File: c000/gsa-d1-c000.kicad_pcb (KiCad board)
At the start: 2 copper layers, 99.7 x 33 mm, 29 parts, among them J301 CONN-4, J302 CONN-3, J303 CONN-3, J304 CONN-3, J305 CONN-3, J306 CONN-3, J307 CONN-2, J308 CONN-3, U301 4066, U302 4066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

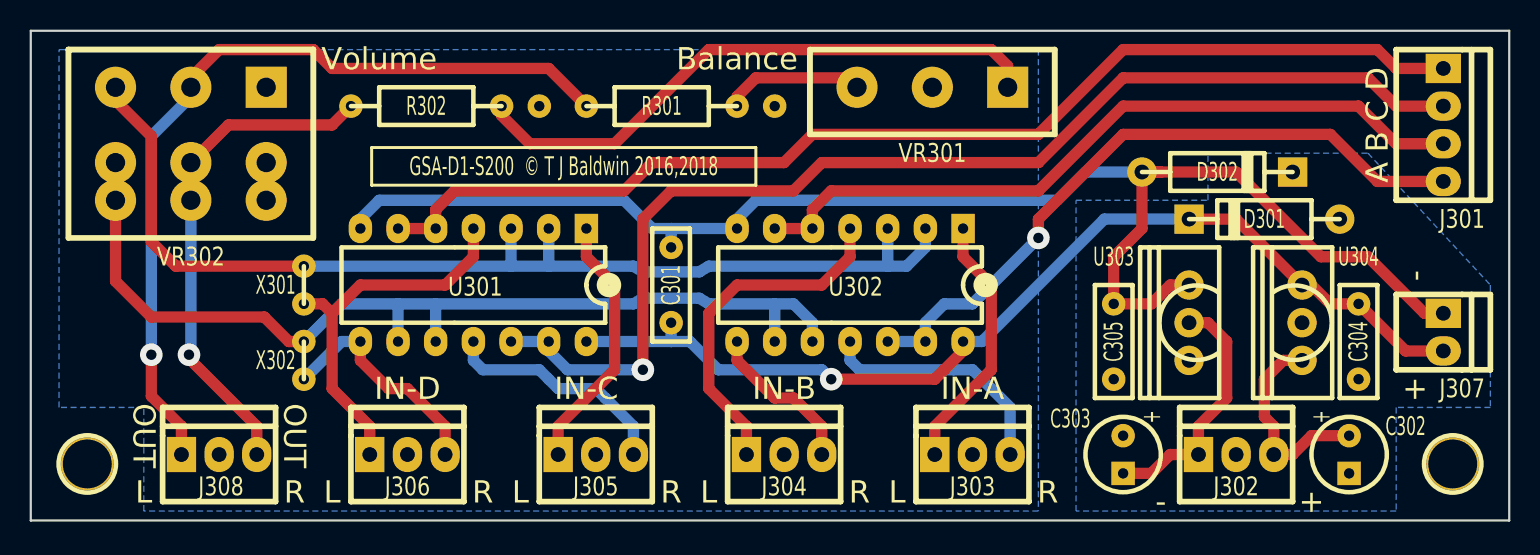
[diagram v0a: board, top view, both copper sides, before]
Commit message: Minor layout improvements to pre-amp controls
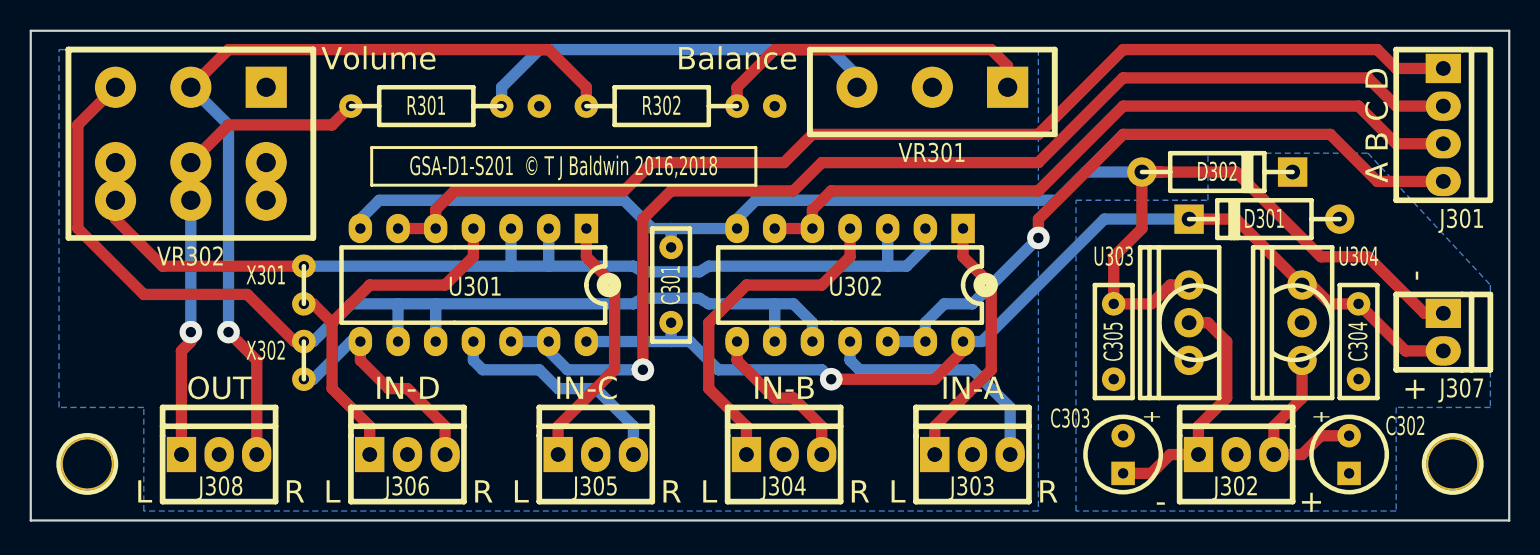
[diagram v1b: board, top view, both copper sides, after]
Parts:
- moved R301 15.9 mm to (120.7, 86.4)
- moved R302 15.9 mm to (136.5, 86.4)
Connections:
- VR302 pad 2: /L-Out -> /R-Out
- VR302 pad 3: /L -> /R
- VR302 pad 5: /R-Out -> /L-Out
- VR302 pad 6: /R -> /L
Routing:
- net /L-Out: track 56.9 -> 33.3 mm
- net /R-Out: track 34.3 -> 56.8 mm
- net Net-(R301-Pad2): track 9.51 -> 27.8 mm
- net Net-(R302-Pad1): track 40.1 -> 23.1 mm
- net /R: track 67.4 -> 73.9 mm
- net /L: track 74.0 -> 69.4 mm
- net /Vin+: track 14.0 -> 12.7 mm
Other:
- board text added: "GSA-D1-S201 © T J Baldwin 2016,2018"
- board text removed: "GSA-D1-S200 © T J Baldwin 2016,2018"

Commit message: Updated to use KiCad v5
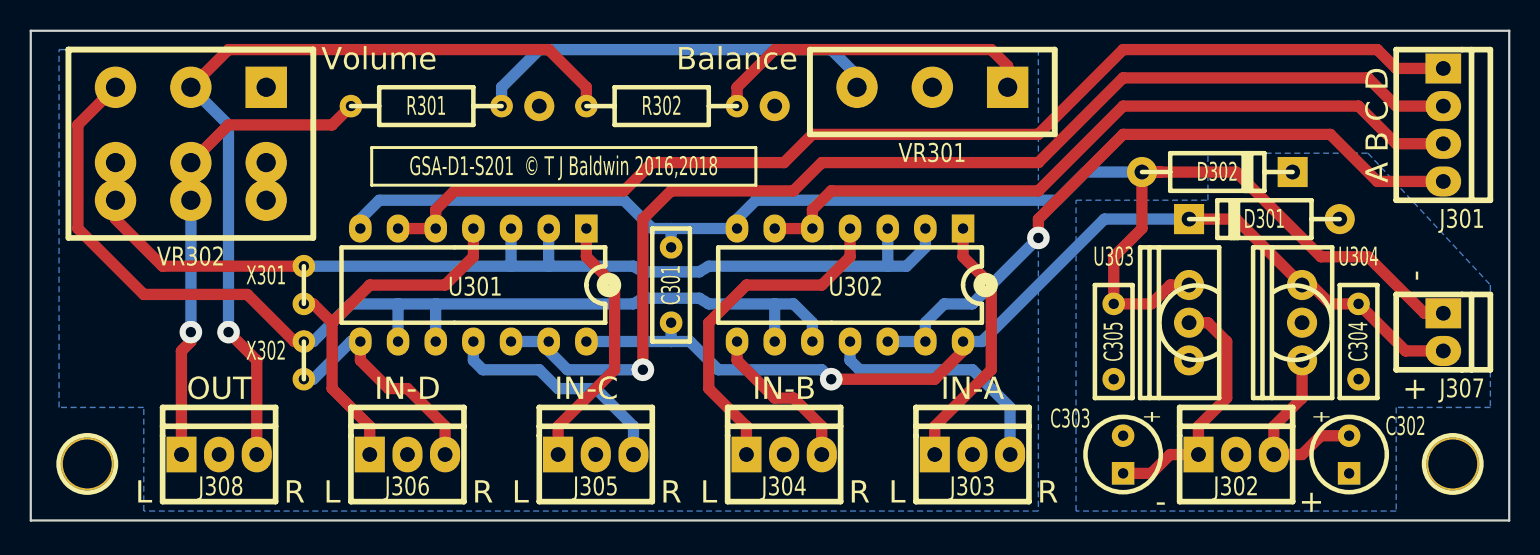
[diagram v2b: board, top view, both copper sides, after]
